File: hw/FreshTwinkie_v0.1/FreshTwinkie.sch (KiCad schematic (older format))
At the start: 50 parts, among them J1 USB_B_Micro, J2 USB_C_Receptacle, P1 USB_C_Plug, Q1 PMDXB600UNE, Q2 PMDXB600UNE, Q3 PMDXB600UNE, Q4 Q_NMOS_DGS, U1 INA231, U2 INA231, U3 NCP167, U4 AD8606ACB, U5 STM32F072CBUx

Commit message: changeFootprintMicro
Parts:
- J1: symbol Connector:USB_B_Micro -> FreshTwinkie-rescue:USB_B_Micro-Connector
- J2: symbol Connector:USB_C_Receptacle -> FreshTwinkie-rescue:USB_C_Receptacle-Connector
- P1: symbol Connector:USB_C_Plug -> FreshTwinkie-rescue:USB_C_Plug-Connector
- U5: footprint Package_DFN_QFN:QFN-48-1EP_7x7mm_P0.5mm_EP5.6x5.6mm -> QFN50P700X700X60-49N(1):QFN50P700X700X60-49N
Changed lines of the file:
@@
 EESchema Schematic File Version 4
-LIBS:FreshTwinkie-cache
-EELAYER 29 0
+EELAYER 30 0
 EELAYER END
 $Descr A3 16535 11693
@@
 $EndDescr
 $Comp
-L Connector:USB_C_Plug P1
+L FreshTwinkie-rescue:USB_C_Plug-Connector P1
 U 1 1 5C99C9A0
 P 2100 8050
@@
 	2700 9350 4150 9350
 $Comp
-L Connector:USB_C_Receptacle J2
+L FreshTwinkie-rescue:USB_C_Receptacle-Connector J2
 U 1 1 5C99EB45
 P 4750 8050
@@
 F 0 "U5" H 13950 6050 50  0000 C CNN
 F 1 "STM32F072CBUx" H 14200 5950 50  0000 C CNN
-F 2 "Package_DFN_QFN:QFN-48-1EP_7x7mm_P0.5mm_EP5.6x5.6mm" H 13050 3100 50  0001 R CNN
+F 2 "QFN50P700X700X60-49N(1):QFN50P700X700X60-49N" H 13050 3100 50  0001 R CNN
 F 3 "http://www.st.com/st-web-ui/static/active/en/resource/technical/document/datasheet/DM00090510.pdf" H 13650 4500 50  0001 C CNN
 F 4 "STMicroelectronics" H 13650 4500 50  0001 C CNN "Mfg"
@@
 ADDR: 0X40
 $Comp
-L Connector:USB_B_Micro J1
+L FreshTwinkie-rescue:USB_B_Micro-Connector J1
 U 1 1 5CAB9DC5
 P 2200 2250

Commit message: Redesign schematic
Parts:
- removed Q1, Q2, Q3: PMDXB600UNE, gkl_housings_qfn:DFN1010B-6 (SOT1216), symbol gkl_mosfet:PMDXB600UNE
- removed R1, R2: 0.015, gkl_dipol:4W_R_1206, symbol gkl_misc:4W_R
- removed U1, U2: INA231, gkl_housings_bga:DSBGA-12_1.56x1.39mm_Layout3x4_P0.4mm, symbol gkl_sensor:INA231
- removed U3: NCP167, gkl_housings_son:X2SON_4_1.0x1.0mm, symbol gkl_pmic:NCP167
- removed U4: AD8606ACB, gkl_housings_bga:WLCSP-8 3X3_0.5, symbol gkl_misc:AD8606ACB
- added Q? (x6): FDG6335N, Package_TO_SOT_SMD:SOT-363_SC-70-6, symbol Transistor_FET:FDG6335N
- added R1: 100ohms, gkl_dipol:R_0201, symbol Device:R
- added SW1: SW_Push, symbol Switch:SW_Push
- added TP1: TestPoint, symbol Connector:TestPoint
- added U1, U2: INA260, Package_SO:TSSOP-16_4.4x5mm_P0.65mm, symbol Sensor:INA260
- added U? (x2): AD8620, symbol Amplifier_Operational:AD8620
- added U?: MIC5504-3.3YM5, Package_TO_SOT_SMD:SOT-23-5, symbol Regulator_Linear:MIC5504-3.3YM5
- FB1, FB2: value 600R -> 600Ohms
- Q4: value Q_NMOS_DGS -> BSD840N
- R15, R17: value 200R -> 200Ohm
- R16, R18: value 100R -> 100Ohm
- R19, R20: value 51.1K -> 35.7k
- R22, R24: value 2.12K -> 4.75k
- R3, R4: value 381K -> 35.7k
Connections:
- net CC1_EN is gone; now on net GND: R3.1, U5.10 (PA0)
- net CC2_EN is gone; now on net GND: R4.1, U5.12 (PA2)
- net USB_B_VBUS is gone; now on net +3V3: R19.1, R20.1
- net +3V3: now also FB2.1, U1.10 (VS), U2.10 (VS), U2.5 (A0), U?.5 (VOUT); no longer FB2.2
- net CC1_BUF: now also U?.1, U?.2 (-)
- net CC1_TX_DATA: now also Q?.2 (G)
- net CC1_TX_EN: now also Q?.5 (G)
- net CC2_BUF: now also U?.6 (-), U?.7
- net CC2_TX_DATA: now also Q?.2 (G)
- net CC2_TX_EN: now also Q?.5 (G)
- net GND: now also Q?.4 (S), Q?.4 (S), R1.2, U1.11 (GND), U1.4 (A1), U1.5 (A0), U1.6 (GND), U2.11 (GND), U2.4 (A1), U2.6 (GND), U?.2 (GND); no longer R3.2, R4.2
- net NRST: now also TP1.1
- net SCL: now also U1.9 (SCL), U2.9 (SCL)
- net SDA: now also U1.8 (SDA), U2.8 (SDA)
- net USB_B_ID: now also SW1.2
- net VBUS_ALERT_L: now also U1.7 (ALERT)
- net VBUS_PLUG: now reaches P1.A4 (VBUS), P1.A9 (VBUS), P1.B4 (VBUS), P1.B9 (VBUS)
- net VBUS_PLUG: now also U1.1 (IN+), U1.12 (VBUS), U1.2 (IN+), U1.3 (IN+)
- net CC2_PLUG: now reaches P1.B5 (VCONN)
- net CC2_PLUG: now also U2.1 (IN+), U2.12 (VBUS), U2.2 (IN+), U2.3 (IN+)
- net VBUS_RECEP: now reaches J2.A4 (VBUS), J2.A9 (VBUS), J2.B4 (VBUS), J2.B9 (VBUS)
- net VBUS_RECEP: now also U1.14 (IN-), U1.15 (IN-), U1.16 (IN-)
- net CC1: now reaches R11.2, R13.2, R16.1, R5.2, R7.2, R9.2
- net CC1: now also Q?.1 (S), Q?.1 (S), U?.3 (+)
- net CC2: now reaches R10.2, R12.2, R14.2, R18.1, R6.2, R8.2
- net CC2: now also Q?.1 (S), Q?.4 (S), U?.5 (+)
- net at R16.2: now also Q?.3 (D)
- net at R15.2: now also Q?.6 (D)
- net at R18.2: now also Q?.3 (D)
- net at R17.2: now also Q?.6 (D)
- net at C5.1, C6.1, U5.9 (VDDA): now also FB2.2; no longer FB2.1
- net at C1.1, FB1.1: now also U?.1 (VIN), U?.3 (EN)
- net USB_C_CC1 renamed CC1_RECEP
- net CC1_RECEP: now also Q?.6 (D)
- net USB_C_CC2 renamed CC2_RECEP
- net CC2_RECEP: now also Q?.3 (D), U2.14 (IN-), U2.15 (IN-), U2.16 (IN-)
- net USB_C_D_N renamed USBC_D-
- net USB_C_D_P renamed USBC_D+
- net USB_C_SBU1 renamed SBUS1
- net USB_C_SBU2 renamed SBUS2
- net USB_C_SSRX1_N renamed RX1-
- net USB_C_SSRX1_P renamed RX1+
- net USB_C_SSRX2_N renamed RX2-
- net USB_C_SSRX2_P renamed RX2+
- net USB_C_SSTX1_N renamed TX1-
- net USB_C_SSTX1_P renamed TX1+
- net USB_C_SSTX2_N renamed TX2-
- net USB_C_SSTX2_P renamed TX2+
- new net: Q?.2 (G), R3.2
- new net: Q?.5 (G), R4.2
- new net: R1.1, SW1.1
- new net VCONN_ALERT_L: U2.7 (ALERT)
- no-connect marks 0 -> 5
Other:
- note added: "CC1/CC2\n"
- note added: "Leds indicadores\n\n"
- note added: "Micro STM32F072CBU\n"
- note added: "Micro-B y regulador de voltaje\n\n"
- note added: "Modo Bootloader\n"
- note added: "Para entrar en el modo boot, \nconectar un cable A-to-A en un adaptador OGT \no usar un cable Micro-B y mientrás se inserta, \npresionar el SW1."
- note added: "USB-C Plug \n& Receptacle\n"
- note removed: "ADDR: 0X40"
- note removed: "ADDR: 0X41\n"
- note removed: "RP resistors to 3v3"
- note removed: "Route as \nKelvin Conections"
- note removed: "Use OTG + A -to- A Cable to boot"
- moved on the sheet: C1, C2, C3, C4, C5, C6, C7, C8, D1, D2, FB1, FB2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

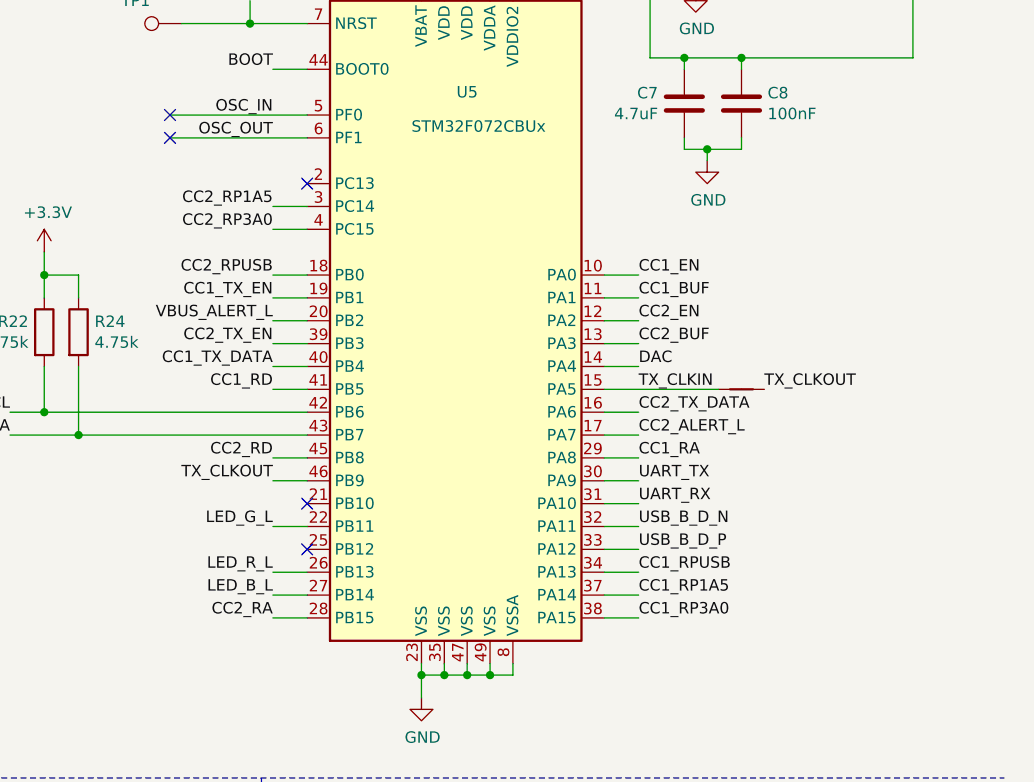
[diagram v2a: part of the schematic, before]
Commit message: ChangePinsMicro
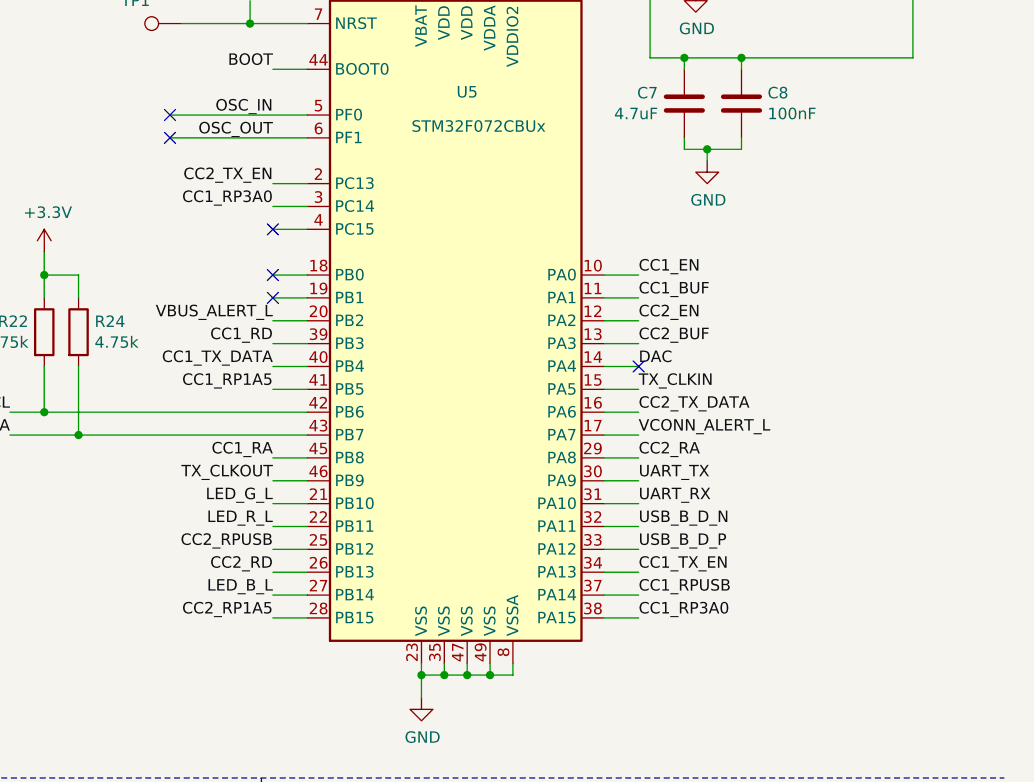
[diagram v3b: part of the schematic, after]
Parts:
- removed NT1: Net-Tie_2, NetTie:NetTie-2_SMD_Pad0.5mm, symbol Device:Net-Tie_2
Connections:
- net CC2_ALERT_L is gone; now on net VCONN_ALERT_L: U5.17 (PA7)
- net CC1_RA: now also U5.45 (PB8); no longer U5.29 (PA8)
- net CC1_RD: now also U5.39 (PB3); no longer U5.41 (PB5)
- net CC1_RP1A5: now also U5.41 (PB5); no longer U5.37 (PA14)
- net CC1_RP3A0: now also U5.3 (PC14)
- net CC1_RPUSB: now also U5.37 (PA14); no longer U5.34 (PA13)
- net CC1_TX_EN: now also U5.34 (PA13); no longer U5.19 (PB1)
- net CC2_RA: now also U5.29 (PA8); no longer U5.28 (PB15)
- net CC2_RD: now also U5.26 (PB13); no longer U5.45 (PB8)
- net CC2_RP1A5: now also U5.28 (PB15); no longer U5.3 (PC14)
- net CC2_RP3A0: no longer U5.4 (PC15)
- net CC2_RPUSB: now also U5.25 (PB12); no longer U5.18 (PB0)
- net CC2_TX_EN: now also U5.2 (PC13); no longer U5.39 (PB3)
- net LED_G_L: now also U5.21 (PB10); no longer U5.22 (PB11)
- net LED_R_L: now also U5.22 (PB11); no longer U5.26 (PB13)
- no-connect marks 5 -> 6
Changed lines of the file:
@@
 CC2_TX_DATA
 Text Label 14450 4700 0    50   ~ 0
-CC2_ALERT_L
+VCONN_ALERT_L
 Text Label 14450 4800 0    50   ~ 0
-CC1_RA
+CC2_RA
 Text Label 14450 4900 0    50   ~ 0
 UART_TX
@@
 USB_B_D_P
 Text Label 14450 5300 0    50   ~ 0
-CC1_RPUSB
-Text Label 14450 5400 0    50   ~ 0
-CC1_RP1A5
+CC1_TX_EN
 Text Label 14450 5500 0    50   ~ 0
 CC1_RP3A0
 Wire Wire Line
 	13000 4000 12850 4000
-Text Label 12850 4000 2    50   ~ 0
-CC2_RPUSB
 Wire Wire Line
 	13000 4100 12850 4100
@@
 Wire Wire Line
 	13000 5500 12850 5500
-Text Label 12850 4100 2    50   ~ 0
-CC1_TX_EN
 Text Label 12850 4200 2    50   ~ 0
 VBUS_ALERT_L
 Text Label 12850 4300 2    50   ~ 0
-CC2_TX_EN
+CC1_RD
 Text Label 12850 4400 2    50   ~ 0
 CC1_TX_DATA
 Text Label 12850 4500 2    50   ~ 0
-CC1_RD
+CC1_RP1A5
 Text Label 12850 4800 2    50   ~ 0
-CC2_RD
+CC1_RA
 Text Label 12850 4900 2    50   ~ 0
 TX_CLKOUT
 Text Label 12850 5100 2    50   ~ 0
-LED_G_L
+LED_R_L
 Text Label 12850 5300 2    50   ~ 0
-LED_R_L
+CC2_RD
 Text Label 12850 5400 2    50   ~ 0
 LED_B_L
 Text Label 12850 5500 2    50   ~ 0
-CC2_RA
+CC2_RP1A5
 Wire Wire Line
 	13000 3700 12850 3700
 Text Label 12850 3700 2    50   ~ 0
-CC2_RP1A5
+CC1_RP3A0
 Wire Wire Line
 	13000 3800 12850 3800
-Text Label 12850 3800 2    50   ~ 0
-CC2_RP3A0
 Text Label 12850 3300 2    50   ~ 0
 OSC_IN
@@
 Text Label 12850 3100 2    50   ~ 0
 BOOT
-Text Label 15000 4500 0    50   ~ 0
-TX_CLKOUT
-$Comp
-L Device:Net-Tie_2 NT1
-U 1 1 5CA6F424
-P 14900 4500
-F 0 "NT1" H 14900 4589 50  0001 C CNN
-F 1 "Net-Tie_2" H 14900 4590 50  0001 C CNN
-F 2 "NetTie:NetTie-2_SMD_Pad0.5mm" H 14900 4500 50  0001 C CNN
-F 3 "~" H 14900 4500 50  0001 C CNN
-	1    14900 4500
-	1    0    0    -1
-$EndComp
-Wire Wire Line
-	14300 4500 14800 4500
 $Comp
 L Device:C C7
@@
 Wire Wire Line
 	12400 3400 13000 3400
-NoConn ~ 13000 3600
-NoConn ~ 13000 5000
-NoConn ~ 13000 5200
+NoConn ~ 12850 3800
 Text Notes 12250 950  0    197  ~ 0
 Micro STM32F072CBU\n
@@
 Text Notes 6050 7400 2    197  ~ 0
 Micro-B y regulador de voltaje\n\n
+Wire Wire Line
+	14300 4500 14450 4500
+NoConn ~ 14450 4400
+Text Label 14450 5400 0    50   ~ 0
+CC1_RPUSB
+Text Label 12850 5200 2    50   ~ 0
+CC2_RPUSB
+Wire Wire Line
+	12850 5200 13000 5200
+Text Label 12850 5000 2    50   ~ 0
+LED_G_L
+Wire Wire Line
+	12850 5000 13000 5000
+NoConn ~ 12850 4100
+NoConn ~ 12850 4000
+Text Label 12850 3600 2    50   ~ 0
+CC2_TX_EN
+Wire Wire Line
+	12850 3600 13000 3600
 $EndSCHEMATC
